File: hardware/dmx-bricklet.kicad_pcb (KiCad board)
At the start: 2 copper layers, 50 x 57.3 mm, 39 parts, among them P1 CON-SENSOR2, P2 BOOT, P3 DMXCON_2x3, SW1 TER, U1 XMC1XXX48, U2 DRILL, U3 DRILL, U4 DRILL, U5 DRILL, U6 ADM3485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

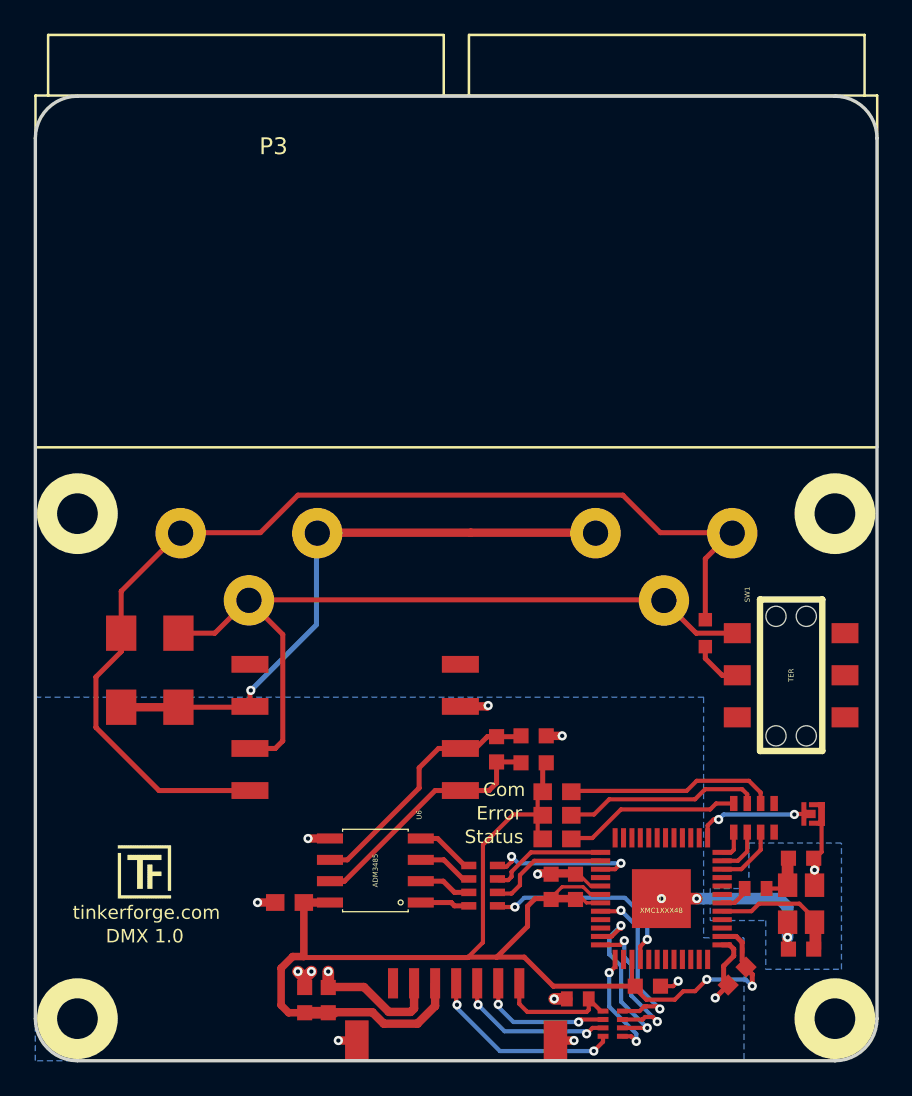
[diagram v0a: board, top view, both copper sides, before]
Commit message: hardware changes
* increase board size to 60x50mm
* add fiducials
* fix all footprints with silkscreen layers
* fix routing after moving connector
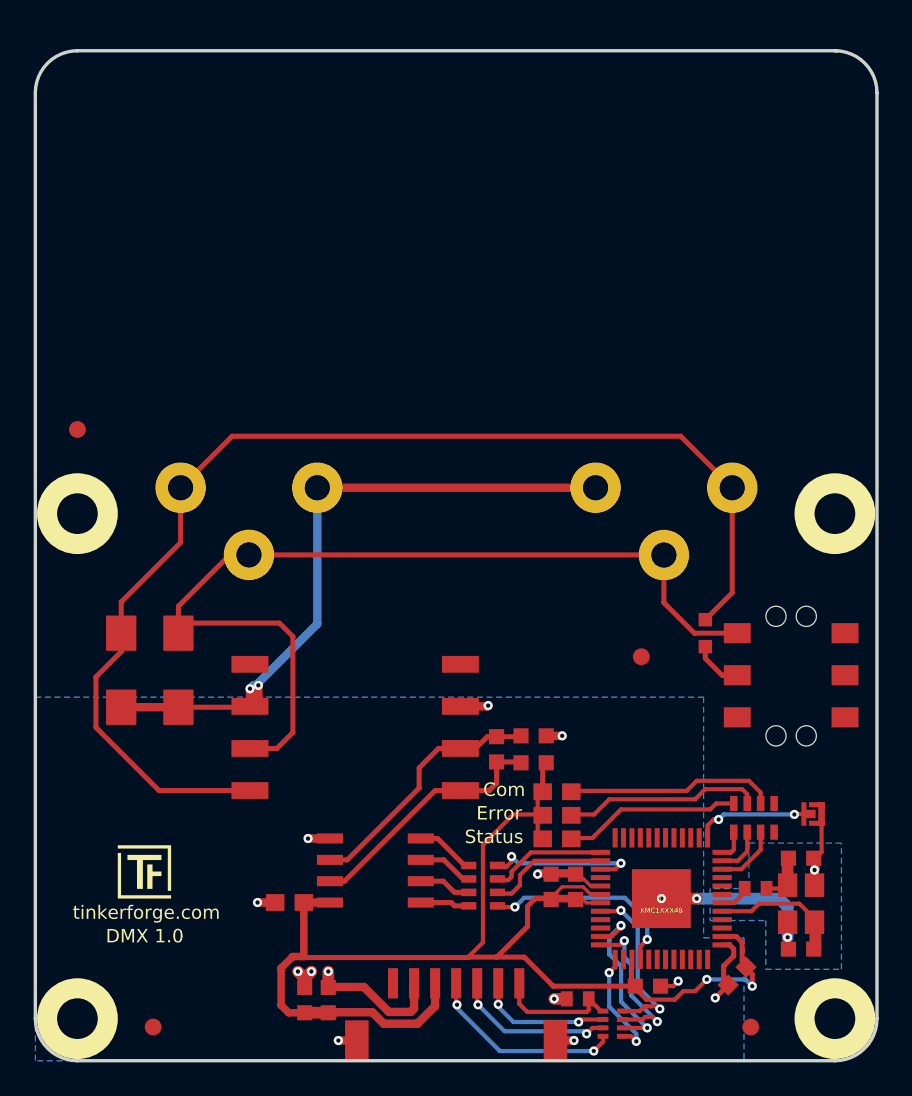
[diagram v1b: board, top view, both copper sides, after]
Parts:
- added Fiducial_Mark: VAL**, kicad-libraries:Fiducial_Mark, F.Cu at (165.6, 119.0)
- added Fiducial_Mark: VAL**, kicad-libraries:Fiducial_Mark, F.Cu at (130.1, 119.0)
- added Fiducial_Mark: VAL**, kicad-libraries:Fiducial_Mark, F.Cu at (159.1, 97.0)
- added Fiducial_Mark: VAL**, kicad-libraries:Fiducial_Mark, F.Cu at (125.6, 83.5)
- moved P3 2.70 mm to (148.1, 57.4)
- moved G*** 2.70 mm to (160.7, 72.2)
- moved G*** 2.70 mm to (135.4, 72.2)
- moved VAL 2.70 mm to (148.1, 72.2)
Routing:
- net Net-(D4-Pad1): track 47.5 -> 55.7 mm
- net Net-(D5-Pad1): track 64.7 -> 70.8 mm
- net Net-(D4-Pad2): track 36.2 -> 40.5 mm, vias 1 -> 2
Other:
- board size 50 x 57.3 mm -> 50 x 60 mm
